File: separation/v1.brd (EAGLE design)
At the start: 71.1 x 26.7 mm, 9 parts, among them IC1 L7805ACV

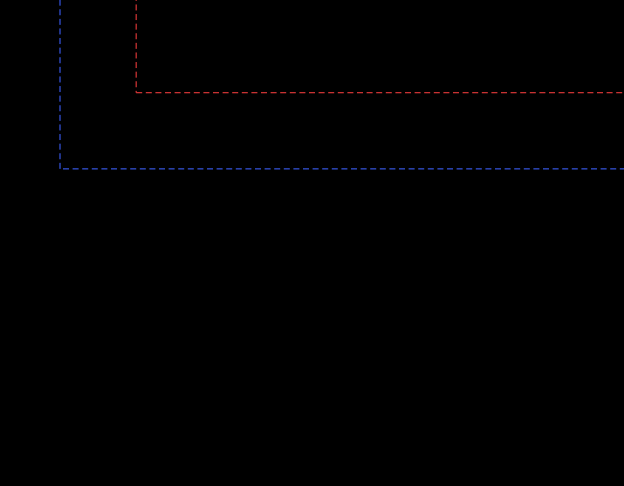
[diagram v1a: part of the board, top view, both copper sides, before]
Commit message: add voltage divider
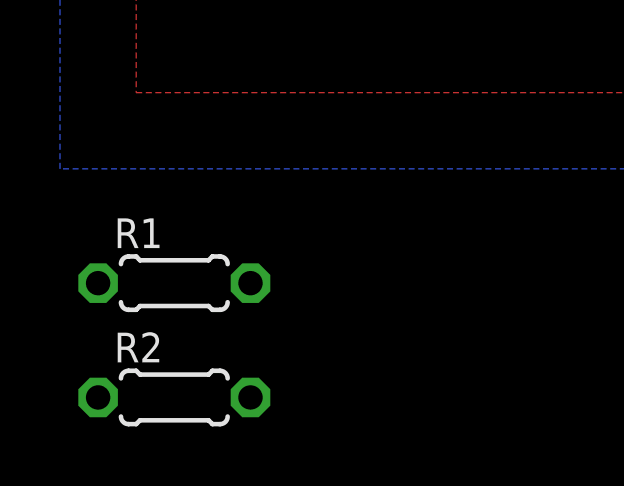
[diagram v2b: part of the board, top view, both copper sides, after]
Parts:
- added R1: 220k, rcl:0204/5
- added R2: 120k, rcl:0204/5
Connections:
- removed net A1: JP2.2
- new net VSENSE: JP2.2, R1.2, R2.1
- net GND: now also R2.2
- net VBAT: now also R1.1
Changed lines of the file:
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@@
 <attribute name="VALUE" x="146.05" y="76.13" size="0.0254" layer="27"/>
+</element>
+<element name="R1" library="rcl" library_urn="urn:adsk.eagle:library:334" package="0204/5" package3d_urn="urn:adsk.eagle:package:23488/1" value="220k" x="76.2" y="41.91" smashed="yes">
+<attribute name="NAME" x="74.1934" y="43.0784" size="0.9906" layer="25" ratio="10"/>
+<attribute name="POPULARITY" value="35" x="76.2" y="41.91" size="1.778" layer="27" display="off"/>
+<attribute name="SPICEPREFIX" value="R" x="76.2" y="41.91" size="1.778" layer="27" display="off"/>
+<attribute name="VALUE" x="74.0664" y="39.5986" size="0.9906" layer="27" ratio="10"/>
+</element>
+<element name="R2" library="rcl" library_urn="urn:adsk.eagle:library:334" package="0204/5" package3d_urn="urn:adsk.eagle:package:23488/1" value="120k" x="76.2" y="38.1" smashed="yes">
+<attribute name="NAME" x="74.1934" y="39.2684" size="0.9906" layer="25" ratio="10"/>
+<attribute name="POPULARITY" value="35" x="76.2" y="38.1" size="1.778" layer="27" display="off"/>
+<attribute name="SPICEPREFIX" value="R" x="76.2" y="38.1" size="1.778" layer="27" display="off"/>
+<attribute name="VALUE" x="74.0664" y="35.7886" size="0.9906" layer="27" ratio="10"/>
 </element>
 </elements>
@@
 </polygon>
 <contactref element="JP6" pad="5"/>
+<contactref element="R2" pad="2"/>
 <wire x1="140.97" y1="72.4" x2="146.05" y2="74.93" width="0" layer="19" extent="1-1"/>
 <wire x1="134.62" y1="72.5805" x2="140.97" y2="72.4" width="0" layer="19" extent="1-1"/>
@@
 <wire x1="113.538" y1="67.691" x2="113.538" y2="62.611" width="0" layer="19" extent="1-1"/>
 <wire x1="94.869" y1="62.738" x2="113.538" y2="62.611" width="0" layer="19" extent="1-1"/>
-</signal>
-<signal name="A1">
-<contactref element="JP2" pad="2"/>
+<wire x1="78.74" y1="38.1" x2="94.869" y2="62.738" width="0" layer="19" extent="1-1"/>
 </signal>
 <signal name="MOSI">
@@
 <wire x1="144.018" y1="58.928" x2="140.208" y2="55.118" width="1.27" layer="16"/>
 <wire x1="140.208" y1="55.118" x2="128.651" y2="55.118" width="1.27" layer="16"/>
+<contactref element="R1" pad="1"/>
+<wire x1="73.66" y1="41.91" x2="128.651" y2="55.118" width="0" layer="19" extent="1-1"/>
 </signal>
 <signal name="BUZZ">
@@
 <wire x1="132.08" y1="58.42" x2="132.08" y2="74.93" width="0.508" layer="1"/>
 </signal>
+<signal name="VSENSE">
+<contactref element="R1" pad="2"/>
+<contactref element="R2" pad="1"/>
+<contactref element="JP2" pad="2"/>
+<wire x1="78.74" y1="41.91" x2="119.38" y2="72.5805" width="0" layer="19" extent="1-1"/>
+<wire x1="73.66" y1="38.1" x2="78.74" y2="41.91" width="0" layer="19" extent="1-1"/>
+</signal>
 </signals>

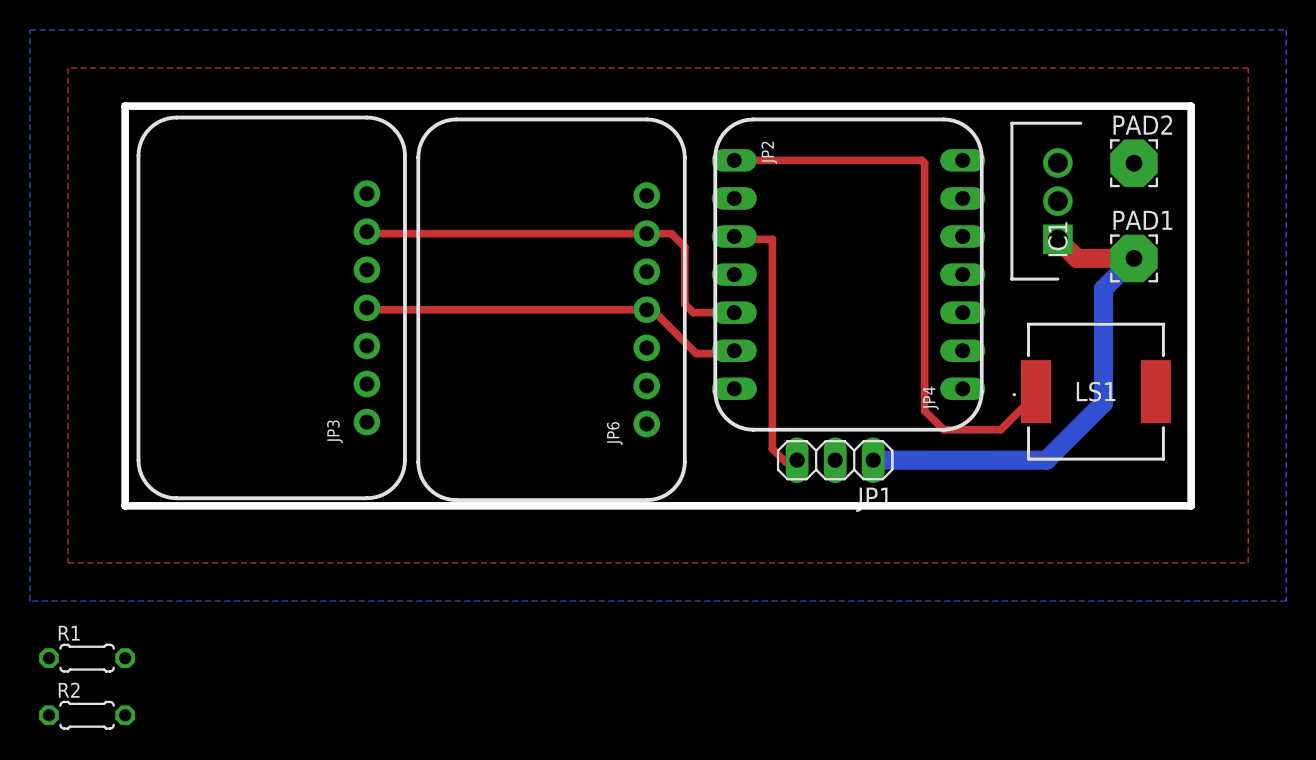
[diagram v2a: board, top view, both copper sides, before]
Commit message: connect resistors
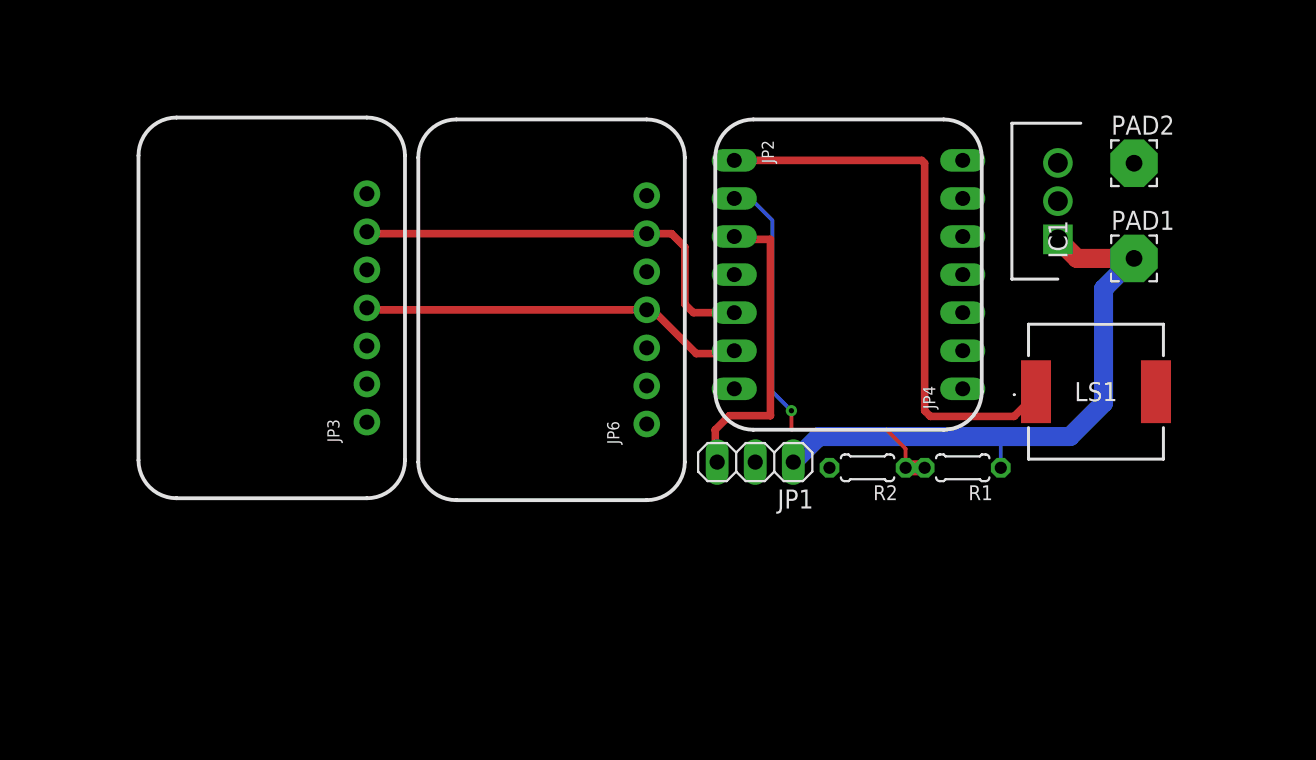
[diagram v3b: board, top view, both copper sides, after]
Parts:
- moved R1 59.8 mm to (134.6, 54.6), turned to 180 degrees
- moved R2 54.6 mm to (128.3, 54.6), turned to 180 degrees
- moved JP1 5.34 mm to (120.8, 55.0)
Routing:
- net VSENSE: track 0.00 -> 28.3 mm, vias 0 -> 1
- net VBAT: track 33.0 -> 40.5 mm
- net SERVO: track 18.9 -> 20.5 mm
- net BUZZ: track 38.4 -> 37.7 mm
- removed copper zone on layer 1, net GND
- removed copper zone on layer 16, net VCC
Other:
- board outline removed

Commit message: reconfigure lower section
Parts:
- moved JP1 12.7 mm to (133.5, 54.7)
- moved R1 8.89 mm to (125.7, 54.4)
- moved R2 8.52 mm to (119.8, 55.0), turned to 145 degrees
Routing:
- net VSENSE: track 28.3 -> 22.1 mm, vias 1 -> 0
- net SERVO: track 20.5 -> 25.3 mm
- net VBAT: track 40.5 -> 38.1 mm
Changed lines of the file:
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@@
 <attribute name="VALUE" x="143.51" y="59.69" size="1.27" layer="27" align="center"/>
 </element>
-<element name="JP1" library="pinhead" library_urn="urn:adsk.eagle:library:325" package="1X03" package3d_urn="urn:adsk.eagle:package:22458/2" value="" x="120.777" y="54.991" smashed="yes" rot="R180">
-<attribute name="NAME" x="124.6632" y="53.1622" size="1.27" layer="25" ratio="10" rot="R180"/>
-<attribute name="POPULARITY" value="92" x="120.777" y="54.991" size="1.778" layer="27" font="vector" ratio="15" rot="R180" display="off"/>
-<attribute name="VALUE" x="124.587" y="58.166" size="1.27" layer="27" rot="R180"/>
+<element name="JP1" library="pinhead" library_urn="urn:adsk.eagle:library:325" package="1X03" package3d_urn="urn:adsk.eagle:package:22458/2" value="" x="133.477" y="54.737" smashed="yes" rot="R180">
+<attribute name="NAME" x="137.3632" y="52.9082" size="1.27" layer="25" ratio="10" rot="R180"/>
+<attribute name="POPULARITY" value="92" x="133.477" y="54.737" size="1.778" layer="27" font="vector" ratio="15" rot="R180" display="off"/>
+<attribute name="VALUE" x="137.287" y="57.912" size="1.27" layer="27" rot="R180"/>
 </element>
 <element name="PAD1" library="wirepad" library_urn="urn:adsk.eagle:library:412" package="3,17/1,1" package3d_urn="urn:adsk.eagle:package:30832/1" value="WIREPAD3,17/1,1" x="146.05" y="68.58" smashed="yes">
@@
 <attribute name="VALUE" x="146.05" y="76.13" size="0.0254" layer="27"/>
 </element>
-<element name="R1" library="rcl" library_urn="urn:adsk.eagle:library:334" package="0204/5" package3d_urn="urn:adsk.eagle:package:23488/1" value="220k" x="134.62" y="54.61" smashed="yes" rot="R180">
-<attribute name="NAME" x="136.6266" y="53.4416" size="0.9906" layer="25" ratio="10" rot="R180"/>
-<attribute name="POPULARITY" value="35" x="134.62" y="54.61" size="1.778" layer="27" rot="R180" display="off"/>
-<attribute name="SPICEPREFIX" value="R" x="134.62" y="54.61" size="1.778" layer="27" rot="R180" display="off"/>
-<attribute name="VALUE" x="136.7536" y="56.9214" size="0.9906" layer="27" ratio="10" rot="R180"/>
+<element name="R1" library="rcl" library_urn="urn:adsk.eagle:library:334" package="0204/5" package3d_urn="urn:adsk.eagle:package:23488/1" value="220k" x="125.73" y="54.356" smashed="yes" rot="R180">
+<attribute name="NAME" x="127.7366" y="53.1876" size="0.9906" layer="25" ratio="10" rot="R180"/>
+<attribute name="POPULARITY" value="35" x="125.73" y="54.356" size="1.778" layer="27" rot="R180" display="off"/>
+<attribute name="SPICEPREFIX" value="R" x="125.73" y="54.356" size="1.778" layer="27" rot="R180" display="off"/>
+<attribute name="VALUE" x="127.8636" y="56.6674" size="0.9906" layer="27" ratio="10" rot="R180"/>
 </element>
-<element name="R2" library="rcl" library_urn="urn:adsk.eagle:library:334" package="0204/5" package3d_urn="urn:adsk.eagle:package:23488/1" value="120k" x="128.27" y="54.61" smashed="yes" rot="R180">
-<attribute name="NAME" x="130.2766" y="53.4416" size="0.9906" layer="25" ratio="10" rot="R180"/>
-<attribute name="POPULARITY" value="35" x="128.27" y="54.61" size="1.778" layer="27" rot="R180" display="off"/>
-<attribute name="SPICEPREFIX" value="R" x="128.27" y="54.61" size="1.778" layer="27" rot="R180" display="off"/>
-<attribute name="VALUE" x="130.4036" y="56.9214" size="0.9906" layer="27" ratio="10" rot="R180"/>
+<element name="R2" library="rcl" library_urn="urn:adsk.eagle:library:334" package="0204/5" package3d_urn="urn:adsk.eagle:package:23488/1" value="120k" x="119.761" y="54.991" smashed="yes" rot="R145">
+<attribute name="NAME" x="120.734540625" y="52.882953125" size="0.9906" layer="25" ratio="10" rot="R145"/>
+<attribute name="POPULARITY" value="35" x="119.761" y="54.991" size="1.778" layer="27" rot="R145" display="off"/>
+<attribute name="SPICEPREFIX" value="R" x="119.761" y="54.991" size="1.778" layer="27" rot="R145" display="off"/>
+<attribute name="VALUE" x="122.8345" y="55.66059375" size="0.9906" layer="27" ratio="10" rot="R145"/>
 </element>
 </elements>
@@
 <wire x1="134.62" y1="72.5805" x2="140.97" y2="72.4" width="0" layer="19" extent="1-1"/>
 <wire x1="147.51" y1="59.69" x2="140.97" y2="72.4" width="0" layer="19" extent="1-1"/>
-<wire x1="120.777" y1="54.991" x2="134.62" y2="72.5805" width="0" layer="19" extent="1-1"/>
-<wire x1="113.538" y1="62.611" x2="120.777" y2="54.991" width="0" layer="19" extent="1-1"/>
+<wire x1="133.477" y1="54.737" x2="147.51" y2="59.69" width="0" layer="19" extent="1-1"/>
+<wire x1="117.680353125" y1="56.44788125" x2="133.477" y2="54.737" width="0" layer="19" extent="1-1"/>
+<wire x1="113.538" y1="62.611" x2="117.680353125" y2="56.44788125" width="0" layer="19" extent="1-1"/>
 <wire x1="113.538" y1="67.691" x2="113.538" y2="62.611" width="0" layer="19" extent="1-1"/>
 <wire x1="94.869" y1="62.738" x2="113.538" y2="62.611" width="0" layer="19" extent="1-1"/>
-<wire x1="125.73" y1="54.61" x2="94.869" y2="62.738" width="0" layer="19" extent="1-1"/>
 </signal>
 <signal name="MOSI">
@@
 <wire x1="119.5705" y1="69.85" x2="119.38" y2="70.0405" width="0.508" layer="1"/>
 <wire x1="119.5705" y1="69.85" x2="121.793" y2="69.85" width="0.508" layer="1"/>
-<wire x1="121.793" y1="58.0851" x2="121.793" y2="69.85" width="0.508" layer="1"/>
-<wire x1="118.237" y1="54.991" x2="118.11" y2="55.118" width="0.508" layer="1"/>
-<wire x1="118.11" y1="55.118" x2="118.11" y2="57.15" width="0.508" layer="1"/>
-<wire x1="119.0451" y1="58.0851" x2="121.793" y2="58.0851" width="0.508" layer="1"/>
-<wire x1="118.11" y1="57.15" x2="119.0451" y2="58.0851" width="0.508" layer="1"/>
+<wire x1="129.413" y1="56.261" x2="130.937" y2="54.737" width="0.508" layer="1"/>
+<wire x1="121.793" y1="69.85" x2="121.793" y2="57.277" width="0.508" layer="1"/>
+<wire x1="121.793" y1="57.277" x2="122.809" y2="56.261" width="0.508" layer="1"/>
+<wire x1="122.809" y1="56.261" x2="129.413" y2="56.261" width="0.508" layer="1"/>
 </signal>
 <signal name="A3">
@@
 <wire x1="144.018" y1="66.548" x2="144.018" y2="58.928" width="1.27" layer="16"/>
 <contactref element="R1" pad="1"/>
-<wire x1="144.018" y1="58.928" x2="141.7828" y2="56.6928" width="1.27" layer="16"/>
-<wire x1="125.0188" y1="56.6928" x2="123.317" y2="54.991" width="1.27" layer="16"/>
-<wire x1="141.7828" y1="56.6928" x2="137.16" y2="56.6928" width="1.27" layer="16"/>
-<wire x1="137.16" y1="56.6928" x2="125.0188" y2="56.6928" width="1.27" layer="16"/>
-<wire x1="137.16" y1="54.61" x2="137.16" y2="56.6928" width="0.254" layer="16"/>
+<wire x1="139.7" y1="54.61" x2="136.144" y2="54.61" width="1.27" layer="16"/>
+<wire x1="136.144" y1="54.61" x2="136.017" y2="54.737" width="1.27" layer="16"/>
+<wire x1="144.018" y1="58.928" x2="139.7" y2="54.61" width="1.27" layer="16"/>
+<wire x1="136.017" y1="54.737" x2="135.89" y2="54.864" width="0.254" layer="16"/>
+<wire x1="135.89" y1="54.864" x2="135.89" y2="57.15" width="0.254" layer="16"/>
+<wire x1="129.54" y1="57.15" x2="128.27" y2="55.88" width="0.254" layer="16"/>
+<wire x1="128.27" y1="55.88" x2="128.27" y2="54.356" width="0.254" layer="16"/>
+<wire x1="135.89" y1="57.15" x2="129.54" y2="57.15" width="0.254" layer="16"/>
 </signal>
 <signal name="BUZZ">
@@
 <contactref element="R2" pad="1"/>
 <contactref element="JP2" pad="2"/>
-<wire x1="130.81" y1="54.61" x2="132.08" y2="54.61" width="1.016" layer="1"/>
-<wire x1="130.81" y1="54.61" x2="130.81" y2="55.88" width="0.254" layer="1"/>
-<wire x1="130.81" y1="55.88" x2="129.54" y2="57.15" width="0.254" layer="1"/>
-<wire x1="123.19" y1="57.15" x2="123.19" y2="58.42" width="0.254" layer="1"/>
-<via x="123.19" y="58.42" extent="1-16" drill="0.35"/>
-<wire x1="123.19" y1="58.42" x2="121.92" y2="59.69" width="0.254" layer="16"/>
 <wire x1="120.4595" y1="72.5805" x2="119.38" y2="72.5805" width="0.254" layer="16"/>
-<wire x1="129.54" y1="57.15" x2="123.19" y2="57.15" width="0.254" layer="1"/>
-<wire x1="121.92" y1="59.69" x2="121.92" y2="71.12" width="0.254" layer="16"/>
-<wire x1="121.92" y1="71.12" x2="120.4595" y2="72.5805" width="0.254" layer="16"/>
+<wire x1="123.19" y1="54.356" x2="123.19" y2="55.88" width="0.508" layer="16"/>
+<wire x1="123.19" y1="55.88" x2="121.92" y2="57.15" width="0.508" layer="16"/>
+<wire x1="121.92" y1="71.12" x2="120.4595" y2="72.5805" width="0.508" layer="16"/>
+<wire x1="121.92" y1="57.15" x2="121.92" y2="71.12" width="0.508" layer="16"/>
+<wire x1="123.19" y1="54.356" x2="122.368115625" y2="53.534115625" width="0.508" layer="16"/>
+<wire x1="122.368115625" y1="53.534115625" x2="121.84164375" y2="53.534115625" width="0.508" layer="16"/>
 </signal>
 </signals>

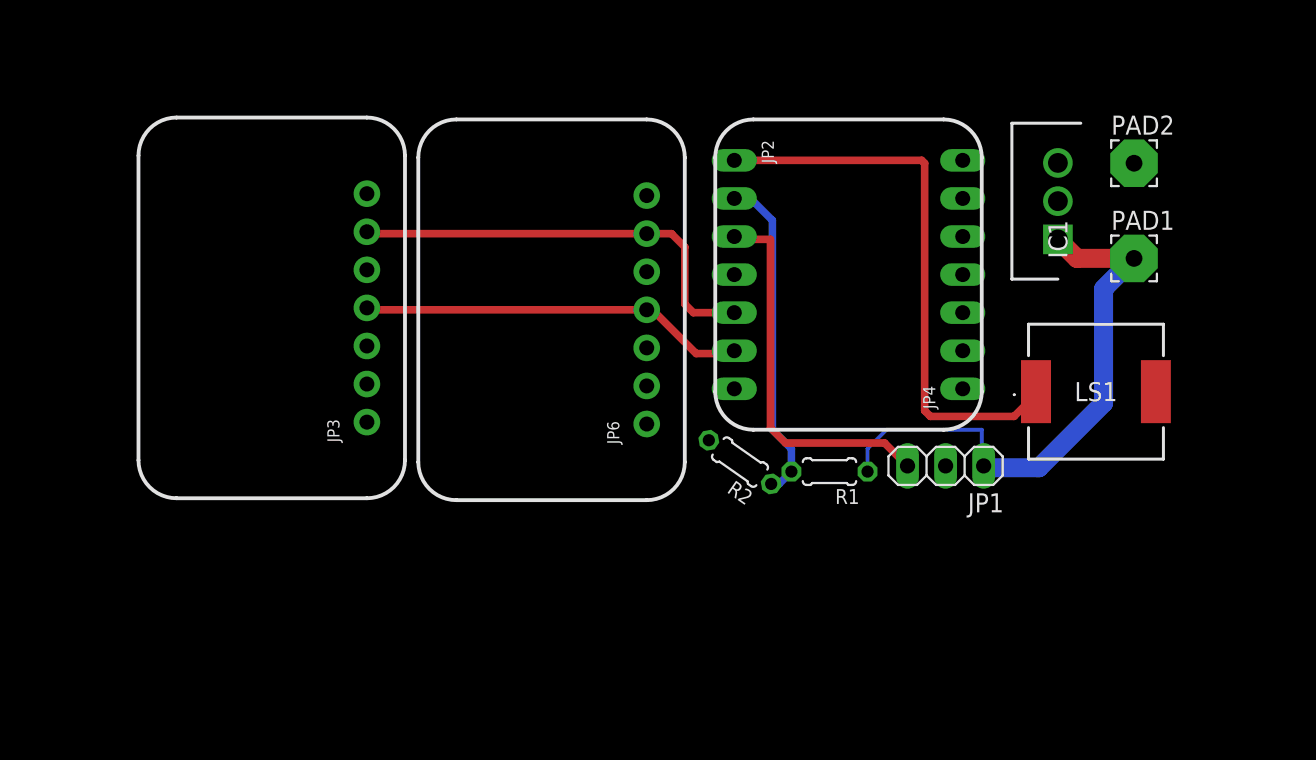
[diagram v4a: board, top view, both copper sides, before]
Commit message: redraw outside dimension
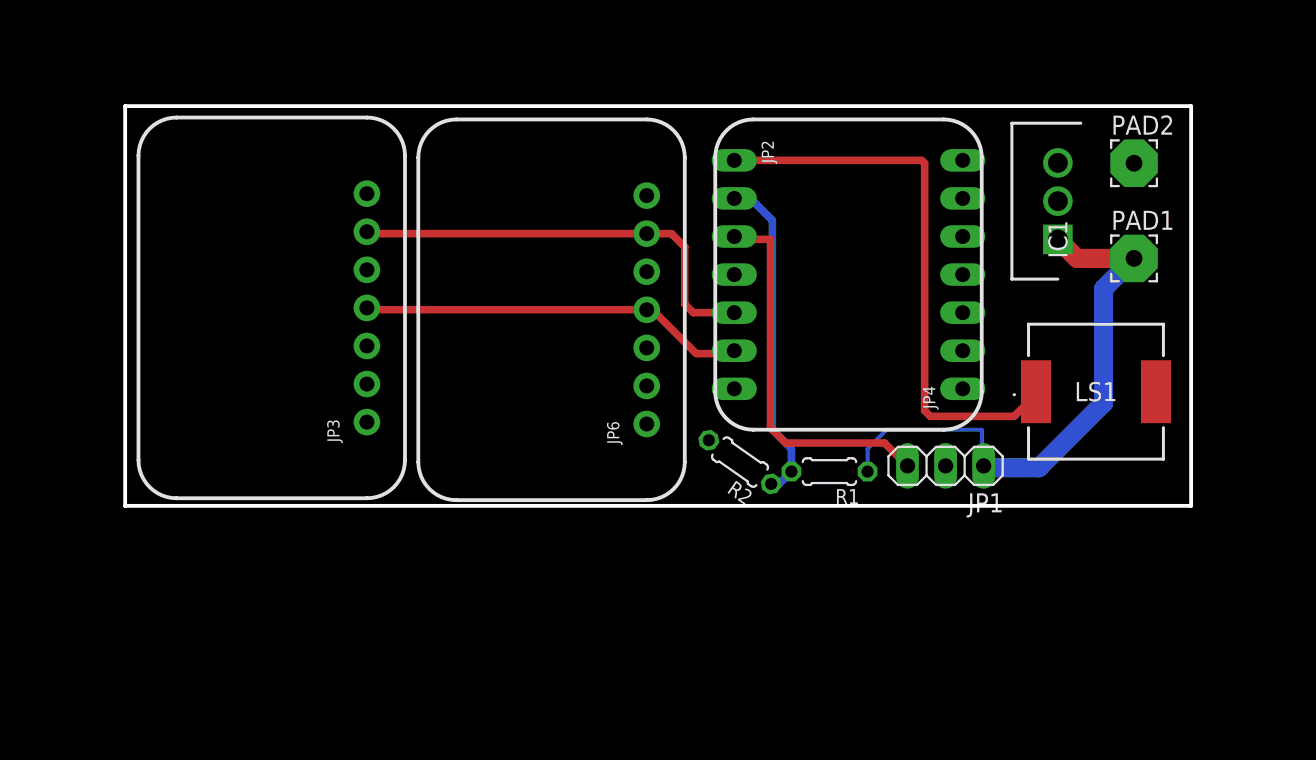
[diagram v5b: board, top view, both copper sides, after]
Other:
- board outline added: 71.1 x 26.7 mm
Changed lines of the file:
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@@
 <wire x1="98.298" y1="75.311" x2="98.298" y2="54.991" width="0.254" layer="21"/>
 <wire x1="98.298" y1="54.991" x2="100.838" y2="52.451" width="0.254" layer="21" curve="90"/>
+<wire x1="78.74" y1="78.74" x2="78.74" y2="52.07" width="0.254" layer="20"/>
+<wire x1="78.74" y1="52.07" x2="149.86" y2="52.07" width="0.254" layer="20"/>
+<wire x1="149.86" y1="52.07" x2="149.86" y2="78.74" width="0.254" layer="20"/>
+<wire x1="149.86" y1="78.74" x2="78.74" y2="78.74" width="0.254" layer="20"/>
 </plain>
 <attributes>
